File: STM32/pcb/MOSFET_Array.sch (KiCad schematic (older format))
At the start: 29 parts, among them U1 HY4903B6, U10 HY4903B6, U11 HY4903B6, U5 HY4903B6, U6 HY4903B6, U7 HY4903B6, U8 HY4903B6, U9 HY4903B6

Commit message: pcb update
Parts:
- added D18, D19, D20, D21: TVS_SMDJ13A, Diode_SMD:D_SMC, symbol Device:D
- added H1, H10, H11, H12, H2, H7, H8, H9: MountingHole_Pad, MountingHole:MountingHole_6mm_Pad_Via, symbol Mechanical:MountingHole_Pad
- R13, R14, R15, R16, R17, R18, R19, R20: value 100 -> 22
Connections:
- net GND: now also D18.2 (A), D19.2 (A), D20.2 (A), D21.2 (A), H10.1, H11.1, H12.1, H9.1
- net OUT-: now also D18.1 (K), D19.1 (K), D20.1 (K), D21.1 (K), H1.1, H2.1, H7.1, H8.1

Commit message: pcb complete
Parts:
- H1, H10, H11, H12, H2, H7, H8, H9: footprint MountingHole:MountingHole_6mm_Pad_Via -> MountingHole:MountingHole_5mm_Pad
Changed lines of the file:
@@
 F 0 "H12" H 5700 2199 50  0000 L CNN
 F 1 "MountingHole_Pad" H 5700 2108 50  0000 L CNN
-F 2 "MountingHole:MountingHole_6mm_Pad_Via" H 5600 2150 50  0001 C CNN
+F 2 "MountingHole:MountingHole_5mm_Pad" H 5600 2150 50  0001 C CNN
 F 3 "~" H 5600 2150 50  0001 C CNN
 	1    5600 2150
@@
 F 0 "H2" H 4450 1499 50  0000 L CNN
 F 1 "MountingHole_Pad" H 4450 1408 50  0000 L CNN
-F 2 "MountingHole:MountingHole_6mm_Pad_Via" H 4350 1450 50  0001 C CNN
+F 2 "MountingHole:MountingHole_5mm_Pad" H 4350 1450 50  0001 C CNN
 F 3 "~" H 4350 1450 50  0001 C CNN
 	1    4350 1450
@@
 F 0 "H10" H 5700 1499 50  0000 L CNN
 F 1 "MountingHole_Pad" H 5700 1408 50  0000 L CNN
-F 2 "MountingHole:MountingHole_6mm_Pad_Via" H 5600 1450 50  0001 C CNN
+F 2 "MountingHole:MountingHole_5mm_Pad" H 5600 1450 50  0001 C CNN
 F 3 "~" H 5600 1450 50  0001 C CNN
 	1    5600 1450
@@
 F 0 "H9" H 5700 1149 50  0000 L CNN
 F 1 "MountingHole_Pad" H 5700 1058 50  0000 L CNN
-F 2 "MountingHole:MountingHole_6mm_Pad_Via" H 5600 1100 50  0001 C CNN
+F 2 "MountingHole:MountingHole_5mm_Pad" H 5600 1100 50  0001 C CNN
 F 3 "~" H 5600 1100 50  0001 C CNN
 	1    5600 1100
@@
 F 0 "H1" H 4450 1149 50  0000 L CNN
 F 1 "MountingHole_Pad" H 4450 1058 50  0000 L CNN
-F 2 "MountingHole:MountingHole_6mm_Pad_Via" H 4350 1100 50  0001 C CNN
+F 2 "MountingHole:MountingHole_5mm_Pad" H 4350 1100 50  0001 C CNN
 F 3 "~" H 4350 1100 50  0001 C CNN
 	1    4350 1100
@@
 F 0 "H11" H 5700 1849 50  0000 L CNN
 F 1 "MountingHole_Pad" H 5700 1758 50  0000 L CNN
-F 2 "MountingHole:MountingHole_6mm_Pad_Via" H 5600 1800 50  0001 C CNN
+F 2 "MountingHole:MountingHole_5mm_Pad" H 5600 1800 50  0001 C CNN
 F 3 "~" H 5600 1800 50  0001 C CNN
 	1    5600 1800
@@
 F 0 "H8" H 4450 2199 50  0000 L CNN
 F 1 "MountingHole_Pad" H 4450 2108 50  0000 L CNN
-F 2 "MountingHole:MountingHole_6mm_Pad_Via" H 4350 2150 50  0001 C CNN
+F 2 "MountingHole:MountingHole_5mm_Pad" H 4350 2150 50  0001 C CNN
 F 3 "~" H 4350 2150 50  0001 C CNN
 	1    4350 2150
@@
 F 0 "H7" H 4450 1849 50  0000 L CNN
 F 1 "MountingHole_Pad" H 4450 1758 50  0000 L CNN
-F 2 "MountingHole:MountingHole_6mm_Pad_Via" H 4350 1800 50  0001 C CNN
+F 2 "MountingHole:MountingHole_5mm_Pad" H 4350 1800 50  0001 C CNN
 F 3 "~" H 4350 1800 50  0001 C CNN
 	1    4350 1800

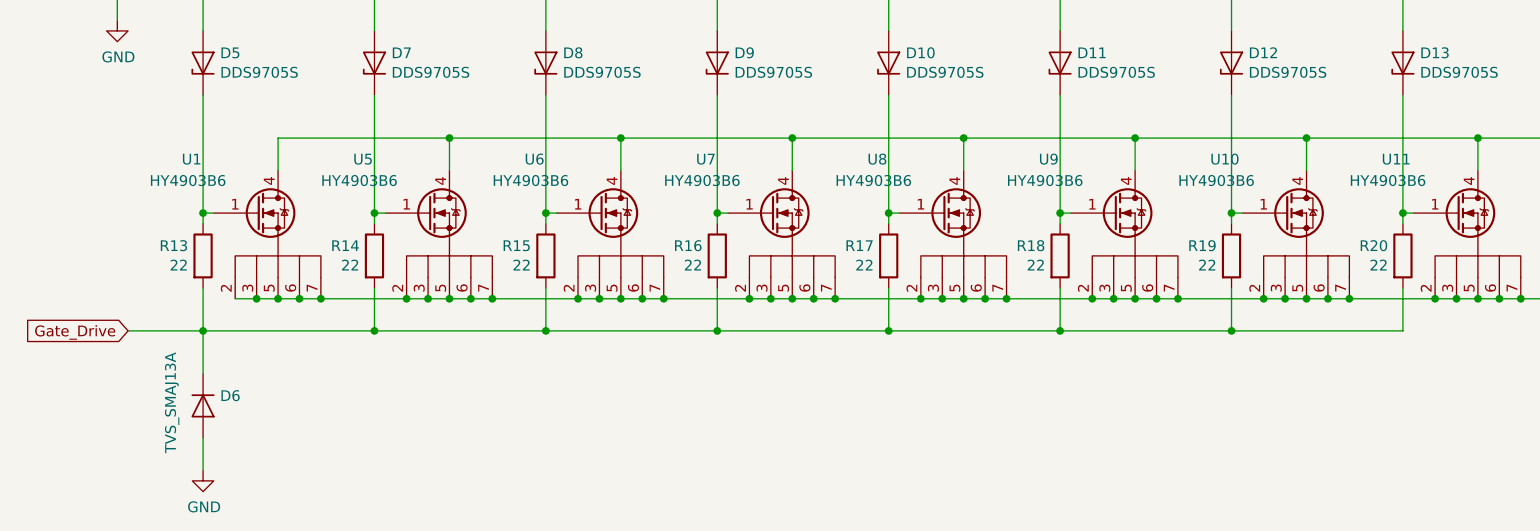
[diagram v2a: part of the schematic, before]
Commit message: gate driver changed to mcp1416
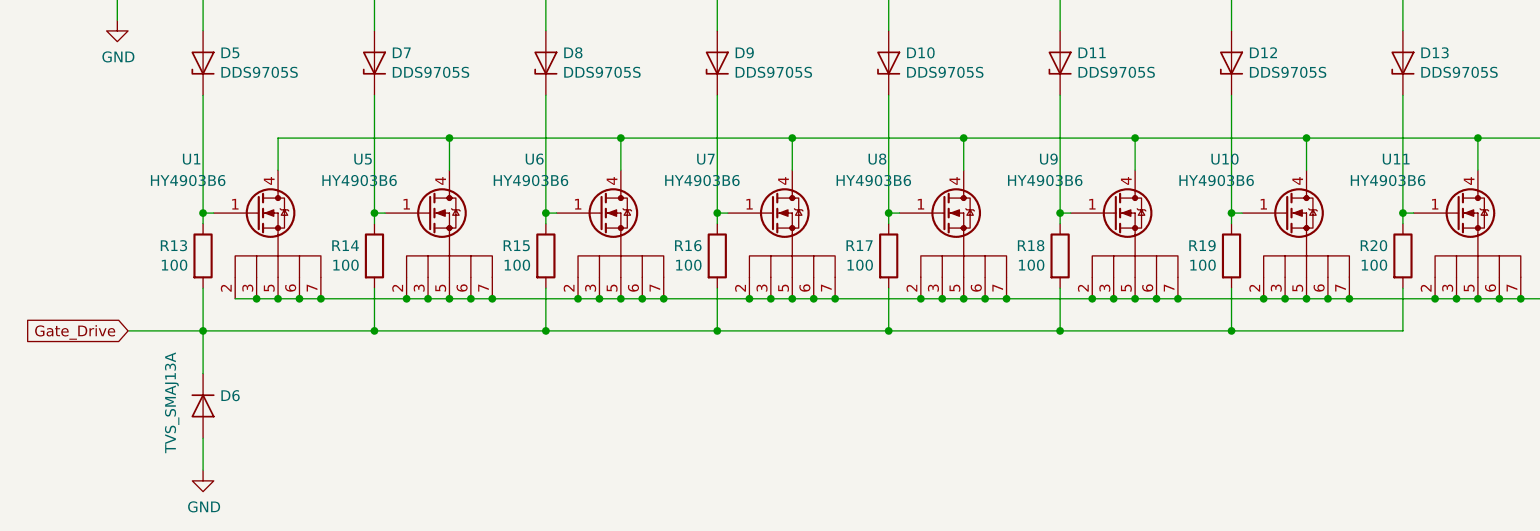
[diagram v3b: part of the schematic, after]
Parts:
- R13, R14, R15, R16, R17, R18, R19, R20: value 22 -> 100
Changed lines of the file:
@@
 P 5200 4050
 F 0 "R16" H 5131 4096 50  0000 R CNN
-F 1 "22" H 5131 4005 50  0000 R CNN
+F 1 "100" H 5131 4005 50  0000 R CNN
 F 2 "Resistor_SMD:R_0603_1608Metric" V 5130 4050 50  0001 C CNN
 F 3 "~" H 5200 4050 50  0001 C CNN
@@
 P 6000 4050
 F 0 "R17" H 5931 4096 50  0000 R CNN
-F 1 "22" H 5931 4005 50  0000 R CNN
+F 1 "100" H 5931 4005 50  0000 R CNN
 F 2 "Resistor_SMD:R_0603_1608Metric" V 5930 4050 50  0001 C CNN
 F 3 "~" H 6000 4050 50  0001 C CNN
@@
 P 3600 4050
 F 0 "R14" H 3531 4096 50  0000 R CNN
-F 1 "22" H 3531 4005 50  0000 R CNN
+F 1 "100" H 3531 4005 50  0000 R CNN
 F 2 "Resistor_SMD:R_0603_1608Metric" V 3530 4050 50  0001 C CNN
 F 3 "~" H 3600 4050 50  0001 C CNN
@@
 P 7600 4050
 F 0 "R19" H 7531 4096 50  0000 R CNN
-F 1 "22" H 7531 4005 50  0000 R CNN
+F 1 "100" H 7531 4005 50  0000 R CNN
 F 2 "Resistor_SMD:R_0603_1608Metric" V 7530 4050 50  0001 C CNN
 F 3 "~" H 7600 4050 50  0001 C CNN
@@
 P 8400 4050
 F 0 "R20" H 8331 4096 50  0000 R CNN
-F 1 "22" H 8331 4005 50  0000 R CNN
+F 1 "100" H 8331 4005 50  0000 R CNN
 F 2 "Resistor_SMD:R_0603_1608Metric" V 8330 4050 50  0001 C CNN
 F 3 "~" H 8400 4050 50  0001 C CNN
@@
 P 2800 4050
 F 0 "R13" H 2731 4096 50  0000 R CNN
-F 1 "22" H 2731 4005 50  0000 R CNN
+F 1 "100" H 2731 4005 50  0000 R CNN
 F 2 "Resistor_SMD:R_0603_1608Metric" V 2730 4050 50  0001 C CNN
 F 3 "~" H 2800 4050 50  0001 C CNN
@@
 P 6800 4050
 F 0 "R18" H 6731 4096 50  0000 R CNN
-F 1 "22" H 6731 4005 50  0000 R CNN
+F 1 "100" H 6731 4005 50  0000 R CNN
 F 2 "Resistor_SMD:R_0603_1608Metric" V 6730 4050 50  0001 C CNN
 F 3 "~" H 6800 4050 50  0001 C CNN
@@
 P 4400 4050
 F 0 "R15" H 4331 4096 50  0000 R CNN
-F 1 "22" H 4331 4005 50  0000 R CNN
+F 1 "100" H 4331 4005 50  0000 R CNN
 F 2 "Resistor_SMD:R_0603_1608Metric" V 4330 4050 50  0001 C CNN
 F 3 "~" H 4400 4050 50  0001 C CNN
